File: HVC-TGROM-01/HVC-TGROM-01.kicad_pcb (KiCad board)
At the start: 2 copper layers, 90.5 x 56.8 mm, 1 part

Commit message: Add extra outlines; Update modules to KiCad 6
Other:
- net class Default removed

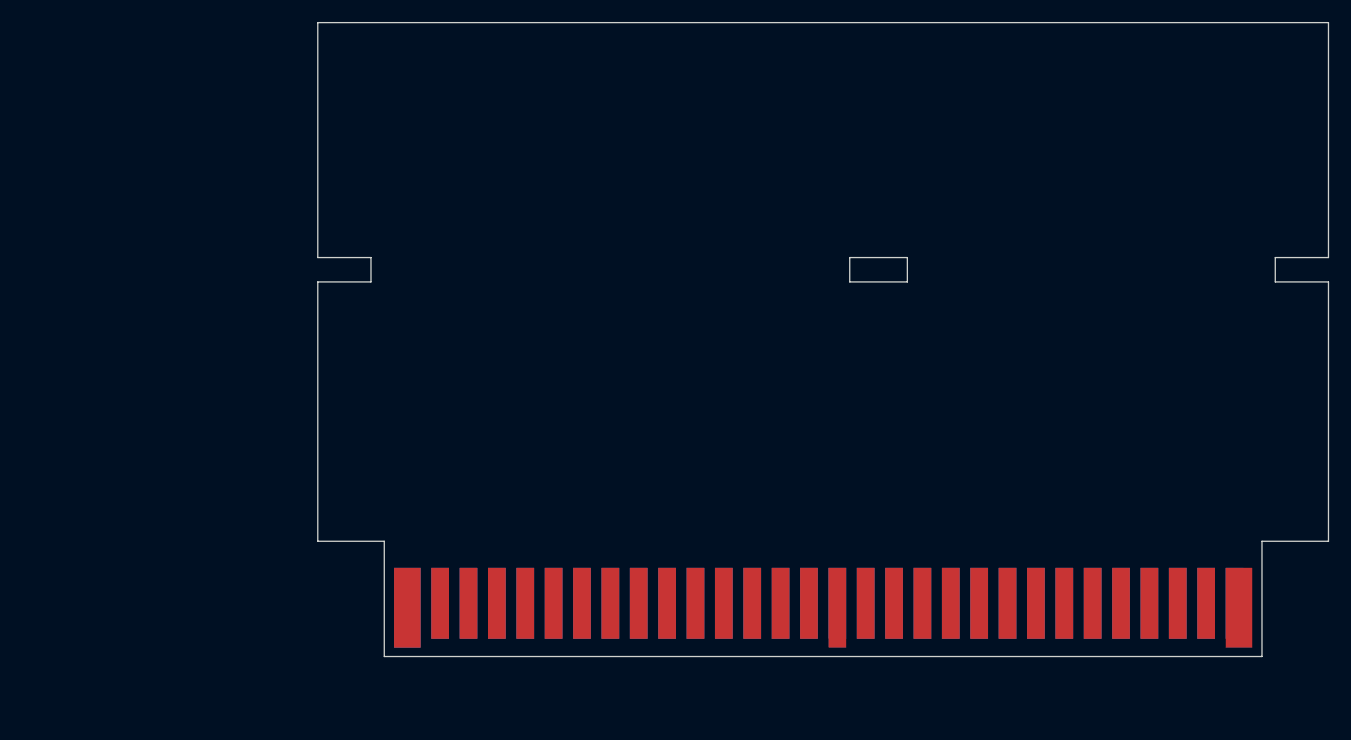
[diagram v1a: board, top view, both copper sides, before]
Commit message: Update HVC-TxROM measurements
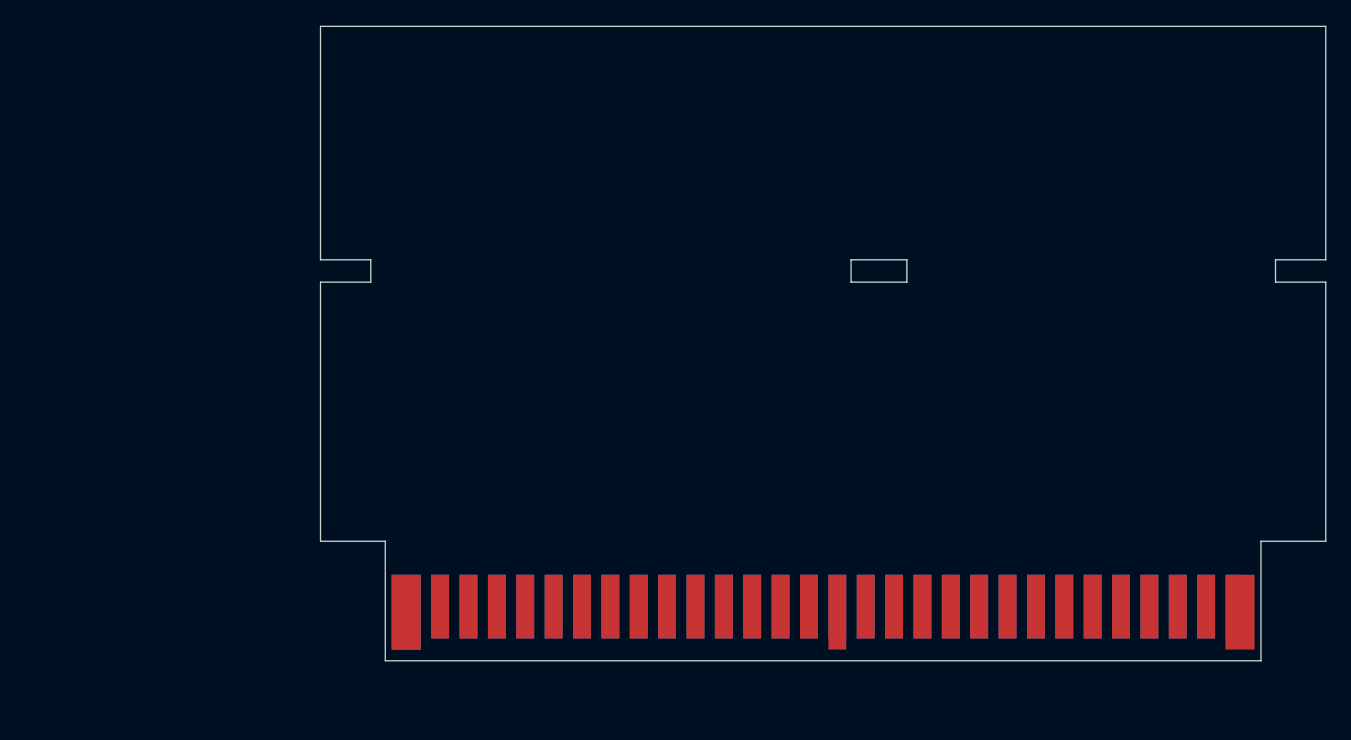
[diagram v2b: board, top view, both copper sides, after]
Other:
- board size 90.5 x 56.8 mm -> 90 x 56.8 mm

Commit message: Update origin to 127, 127 mm
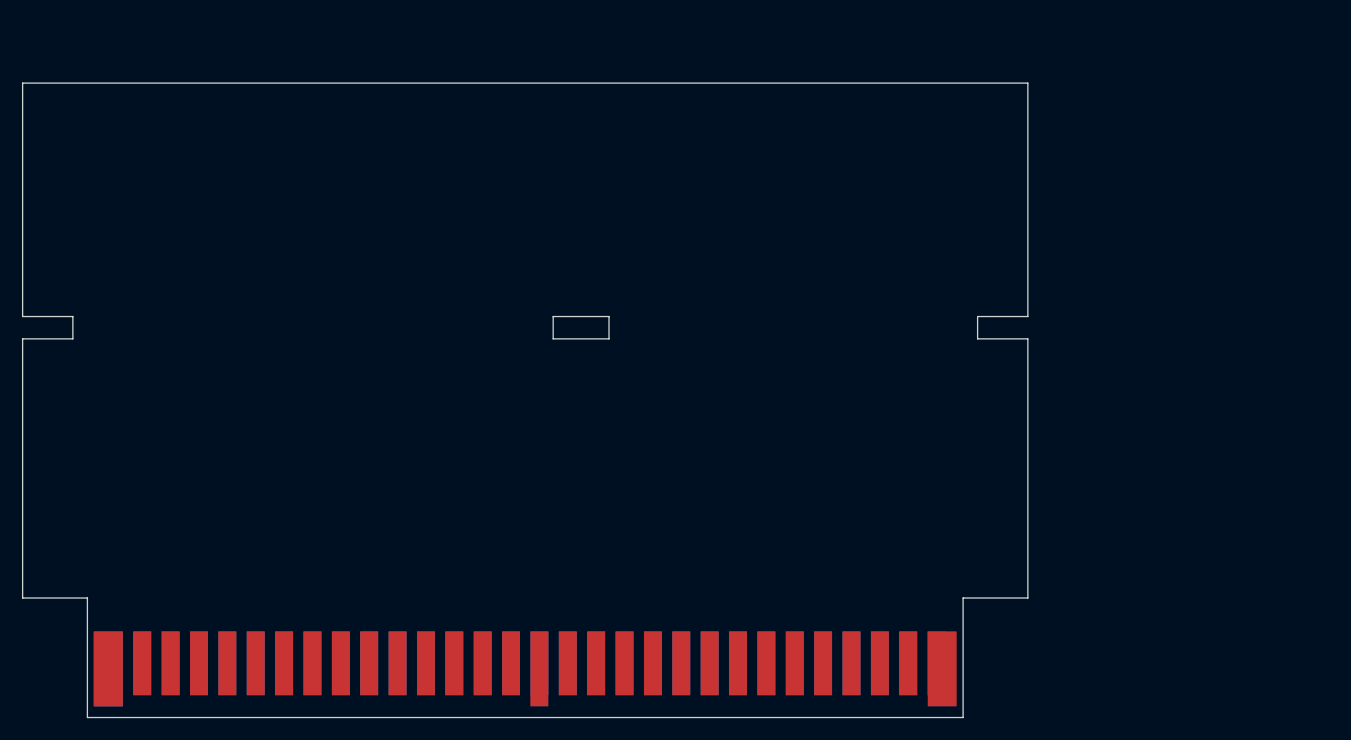
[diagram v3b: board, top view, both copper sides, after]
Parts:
- moved REF** 27.1 mm to (127.0, 127.0)
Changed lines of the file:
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@@
     )
     (pad_to_mask_clearance 0)
-    (grid_origin 153.67 121.92)
+    (grid_origin 127 127)
     (pcbplotparams
       (layerselection 0x00013c0_ffffffff)
@@
   (net 0 "")
   (footprint "card-edge-connectors:HVC-TGROM-01" locked (layer "F.Cu")
-    (at 153.67 121.92)
+    (at 127 127)
     (attr through_hole)
-    (fp_text reference "REF**" (at 0 0) (layer "F.Fab")
+    (fp_text reference "REF**" (at -26.67 5.08) (layer "F.Fab")
       (effects (font (size 1 1) (thickness 0.15)))
     )
-    (fp_text value "HVC-TGROM-01" (at 0 11.43) (layer "F.Fab")
+    (fp_text value "HVC-TGROM-01" (at -26.67 16.51) (layer "F.Fab")
       (effects (font (size 1 1) (thickness 0.15)))
     )
@@
     (pad "60" connect rect locked (at 36.83 5.85) (size 1.6 5.7) (layers "B.Cu"))
   )
-  (gr_line (start 113.17 98.72) (end 113.17 96.72) (layer "Edge.Cuts") (width 0.05))
-  (gr_line (start 194.17 98.72) (end 194.17 96.72) (layer "Edge.Cuts") (width 0.05))
-  (gr_line (start 108.67 96.72) (end 113.17 96.72) (layer "Edge.Cuts") (width 0.05))
-  (gr_line (start 108.67 98.72) (end 108.67 121.92) (layer "Edge.Cuts") (width 0.05))
-  (gr_line (start 194.17 96.72) (end 198.67 96.72) (layer "Edge.Cuts") (width 0.05))
-  (gr_line (start 161.17 96.72) (end 156.17 96.72) (layer "Edge.Cuts") (width 0.05))
-  (gr_line (start 156.17 98.72) (end 161.17 98.72) (layer "Edge.Cuts") (width 0.05))
-  (gr_line (start 161.17 96.72) (end 161.17 98.72) (layer "Edge.Cuts") (width 0.05))
-  (gr_line (start 156.17 98.72) (end 156.17 96.72) (layer "Edge.Cuts") (width 0.05))
-  (gr_line (start 108.67 75.82) (end 108.67 96.72) (layer "Edge.Cuts") (width 0.05))
-  (gr_line (start 114.47 132.62) (end 192.87 132.62) (layer "Edge.Cuts") (width 0.05))
-  (gr_line (start 198.67 98.72) (end 194.17 98.72) (layer "Edge.Cuts") (width 0.05))
-  (gr_line (start 108.67 121.92) (end 114.47 121.92) (layer "Edge.Cuts") (width 0.05))
-  (gr_line (start 192.87 132.62) (end 192.87 121.92) (layer "Edge.Cuts") (width 0.05))
-  (gr_line (start 114.47 121.92) (end 114.47 132.62) (layer "Edge.Cuts") (width 0.05))
-  (gr_line (start 198.67 75.82) (end 108.67 75.82) (layer "Edge.Cuts") (width 0.05))
-  (gr_line (start 192.87 121.92) (end 198.67 121.92) (layer "Edge.Cuts") (width 0.05))
-  (gr_line (start 198.67 121.92) (end 198.67 98.72) (layer "Edge.Cuts") (width 0.05))
-  (gr_line (start 113.17 98.72) (end 108.67 98.72) (layer "Edge.Cuts") (width 0.05))
-  (gr_line (start 198.67 96.72) (end 198.67 75.82) (layer "Edge.Cuts") (width 0.05))
+  (gr_line (start 86.5 103.8) (end 86.5 101.8) (layer "Edge.Cuts") (width 0.05))
+  (gr_line (start 167.5 103.8) (end 167.5 101.8) (layer "Edge.Cuts") (width 0.05))
+  (gr_line (start 82 101.8) (end 86.5 101.8) (layer "Edge.Cuts") (width 0.05))
+  (gr_line (start 82 103.8) (end 82 127) (layer "Edge.Cuts") (width 0.05))
+  (gr_line (start 167.5 101.8) (end 172 101.8) (layer "Edge.Cuts") (width 0.05))
+  (gr_line (start 134.5 101.8) (end 129.5 101.8) (layer "Edge.Cuts") (width 0.05))
+  (gr_line (start 129.5 103.8) (end 134.5 103.8) (layer "Edge.Cuts") (width 0.05))
+  (gr_line (start 134.5 101.8) (end 134.5 103.8) (layer "Edge.Cuts") (width 0.05))
+  (gr_line (start 129.5 103.8) (end 129.5 101.8) (layer "Edge.Cuts") (width 0.05))
+  (gr_line (start 82 80.9) (end 82 101.8) (layer "Edge.Cuts") (width 0.05))
+  (gr_line (start 87.8 137.7) (end 166.2 137.7) (layer "Edge.Cuts") (width 0.05))
+  (gr_line (start 172 103.8) (end 167.5 103.8) (layer "Edge.Cuts") (width 0.05))
+  (gr_line (start 82 127) (end 87.8 127) (layer "Edge.Cuts") (width 0.05))
+  (gr_line (start 166.2 137.7) (end 166.2 127) (layer "Edge.Cuts") (width 0.05))
+  (gr_line (start 87.8 127) (end 87.8 137.7) (layer "Edge.Cuts") (width 0.05))
+  (gr_line (start 172 80.9) (end 82 80.9) (layer "Edge.Cuts") (width 0.05))
+  (gr_line (start 166.2 127) (end 172 127) (layer "Edge.Cuts") (width 0.05))
+  (gr_line (start 172 127) (end 172 103.8) (layer "Edge.Cuts") (width 0.05))
+  (gr_line (start 86.5 103.8) (end 82 103.8) (layer "Edge.Cuts") (width 0.05))
+  (gr_line (start 172 101.8) (end 172 80.9) (layer "Edge.Cuts") (width 0.05))
 )
